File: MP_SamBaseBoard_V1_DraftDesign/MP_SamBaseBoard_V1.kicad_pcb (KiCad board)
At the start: 2 copper layers, 175 x 130.2 mm, 265 parts, among them J1 MOTOR-A_CONN, J10 P1_CONN, J11 I2C_CONN, J12 I2C_CONN, J13 SAM_SWD, J14 WS2812_EXT, J15 PWR_JACK, J16 USB_B_Micro, J17 BATT_CONN, J2 MOTOR-B_CONN, J3 Adafruit_Feather_CONN, J4 uSD_Card, J5 Conn_01x02, J6 Conn_01x02, J7 SERVO_CONN, J8 P3_CONN, J9 P2_CONN, Q1 DMP3098L, SW1 RESET, SW2 3v3_PWR_SW, SW3 SW1, SW4 SW2, U1 ESP32-WROOM-32, U10 MPU-6050, U11 IRFHM9331PbF, U12 BD5291FVE-GTR, U2 ATSAMD51J19A-A, U3 74LVC1G125, U4 TPS62135, U5 TPS62086, U6 MAX98357AETE, U7 DRV8833RTY, U8 HDC1080, U9 MCP73871-1CC, Y1 Crystal

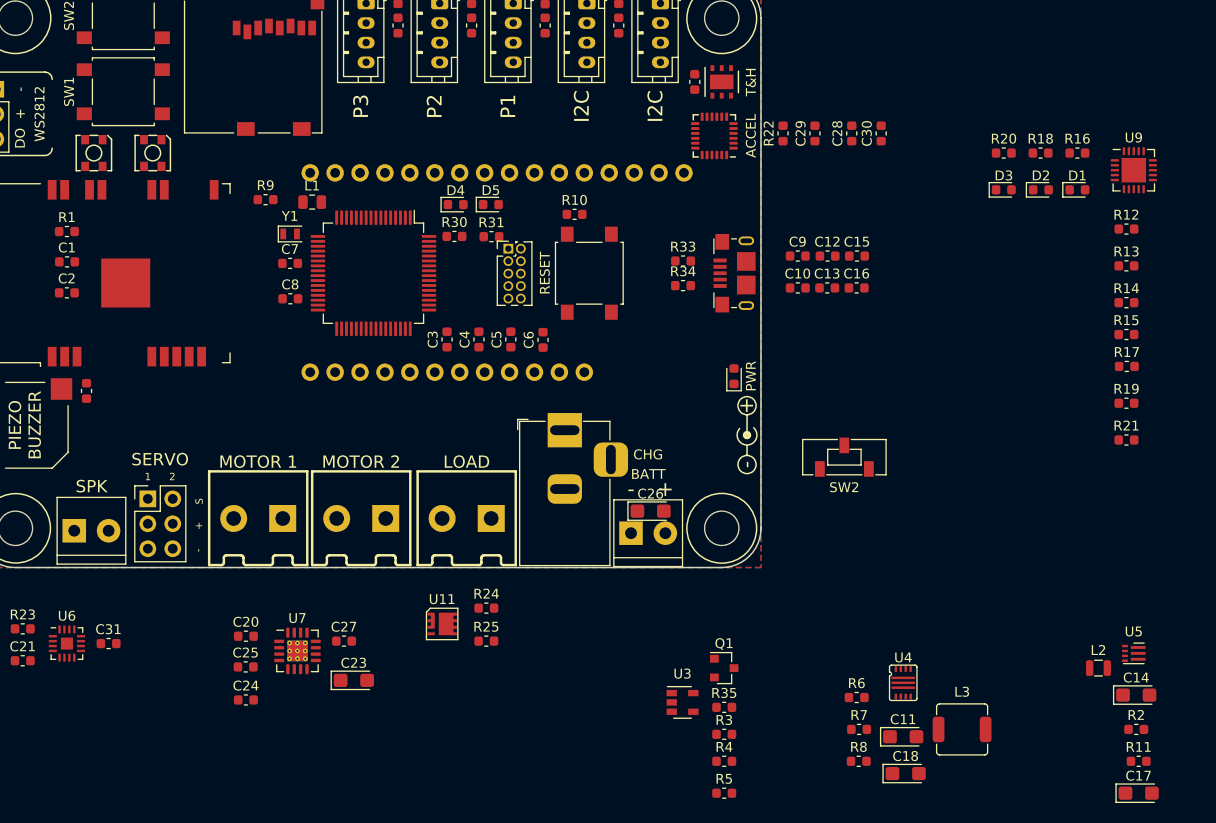
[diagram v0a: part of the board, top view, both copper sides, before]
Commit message: Progress in PCB, QSPI flash not complete in schematics
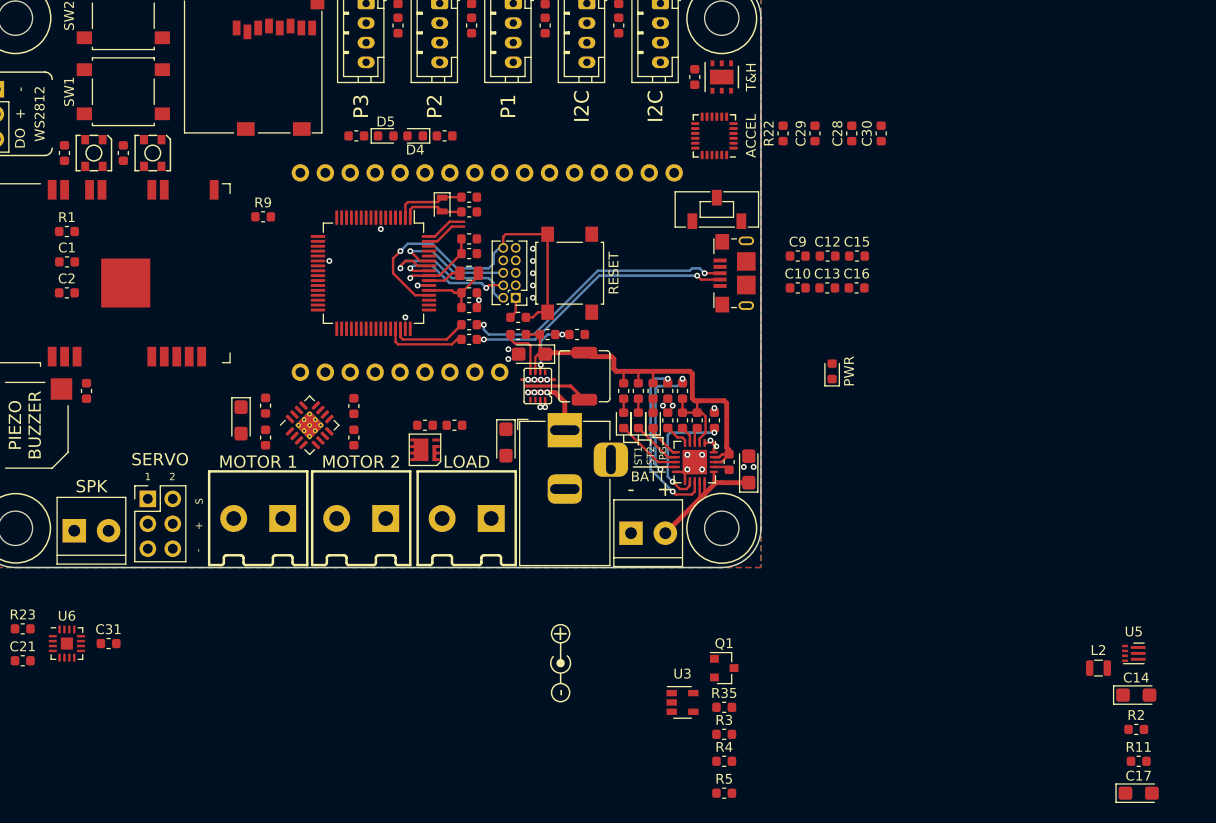
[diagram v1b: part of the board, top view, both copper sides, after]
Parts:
- added C42: 1uF, Capacitor_SMD:C_0603_1608Metric, F.Cu at (178.8, 180.5)
- added C43: 1uF, Capacitor_SMD:C_0603_1608Metric, F.Cu at (184.8, 180.5)
- J3: footprint GiraffeTech-Connector:Adafruit-Feather_WoMountPoint -> GiraffeTech-Connector:Adafruit-Feather_WoMountPoint_TypeA
- moved C18 57.3 mm to (226.4, 201.0), turned to 180 degrees
- moved R8 55.7 mm to (225.0, 199.0), turned to 180 degrees
- moved U9 53.7 mm to (243.0, 212.0), turned to 270 degrees
- moved L3 52.7 mm to (231.8, 203.2), turned to 90 degrees
- moved C11 50.4 mm to (223.8, 210.0), turned to 270 degrees
- moved R16 49.6 mm to (238.8, 204.8), turned to 270 degrees
- moved R7 49.5 mm to (231.0, 199.0)
- moved D1 49.2 mm to (238.8, 207.8), turned to 90 degrees
- moved R18 48.9 mm to (235.8, 204.8), turned to 270 degrees
- moved D2 48.6 mm to (235.8, 207.8), turned to 90 degrees
- moved R6 48.6 mm to (228.0, 199.0)
- moved U4 48.0 mm to (227.0, 204.2), turned to 180 degrees
- moved R13 47.0 mm to (241.8, 204.8), turned to 90 degrees
- moved R12 47.0 mm to (246.5, 212.0), turned to 270 degrees
- moved R14 46.8 mm to (241.8, 207.8), turned to 270 degrees
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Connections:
- J6 pad 1: Net-(J6-Pad1) -> GND
- J6 pad 2: GND -> Net-(J6-Pad2)
- U11 pad 1: Net-(J6-Pad1) -> Net-(J6-Pad2)
- U11 pad 2: Net-(J6-Pad1) -> Net-(J6-Pad2)
- U11 pad 3: Net-(J6-Pad1) -> Net-(J6-Pad2)
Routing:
- net +5V: track 0.00 -> 49.8 mm
- net ~RESET: track 0.00 -> 36.6 mm, vias 0 -> 1
- net Net-(J16-Pad3): track 0.00 -> 28.5 mm, vias 0 -> 2
- net Net-(J16-Pad2): track 0.00 -> 27.6 mm, vias 0 -> 2
- net PROG1: track 0.00 -> 18.1 mm, vias 0 -> 2
- net SWDIO: track 0.00 -> 16.7 mm, vias 0 -> 1
- net +BATT: track 0.00 -> 14.9 mm
- net ~TE: track 0.00 -> 13.9 mm, vias 0 -> 2
- net VIN: track 0.00 -> 13.5 mm, vias 0 -> 4
- net PROG3: track 0.00 -> 12.9 mm, vias 0 -> 2
- net SWO: track 0.00 -> 12.7 mm, vias 0 -> 1
- net SWCLK: track 0.00 -> 12.7 mm, vias 0 -> 2
- net GND: track 0.00 -> 11.3 mm, vias 0 -> 27
- net +3V3: track 0.00 -> 10.2 mm, vias 0 -> 1
- net USB_DM: track 0.00 -> 8.36 mm
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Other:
- board text added: "PG"
- board text added: "ST1"
- board text added: "ST2"

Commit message: update
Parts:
- added U13: SST25VF016B-50-4C-S2AF, Package_SO:SOIC-8_5.275x5.275mm_P1.27mm, F.Cu at (199.5, 192.8)
- J3: footprint GiraffeTech-Connector:Adafruit-Feather_WoMountPoint_TypeA -> GiraffeTech-Connector:Adafruit-Feather_WoMountPoint_TypeB
- moved C17 67.2 mm to (237.5, 201.7), turned to 180 degrees
- moved R11 56.9 mm to (248.0, 202.2)
- moved R2 55.7 mm to (248.0, 200.5)
- moved L2 52.9 mm to (241.5, 201.7), turned to 180 degrees
- moved U5 52.4 mm to (244.8, 201.5), turned to 180 degrees
- moved C14 51.5 mm to (247.2, 204.2)
- moved R4 48.8 mm to (235.8, 194.8)
- moved R5 48.2 mm to (236.5, 198.5), turned to 270 degrees
- moved R3 44.7 mm to (235.8, 196.2), turned to 180 degrees
- moved R35 40.0 mm to (235.0, 198.5), turned to 90 degrees
- moved U3 38.1 mm to (239.2, 198.5)
- moved Q1 34.6 mm to (243.0, 198.5)
- moved C10 31.1 mm to (222.6, 198.1), turned to 270 degrees
- moved C15 19.1 mm to (248.0, 206.2)
- moved C9 19.1 mm to (248.0, 209.2)
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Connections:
- U3 pad 5: VCC -> +3V3
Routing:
- net +3V3: track 10.2 -> 53.0 mm
- net USB_ID: track 0.00 -> 32.4 mm, vias 0 -> 2
- net AREF: track 0.00 -> 30.0 mm
- net CHG_OUT: track 2.27 -> 30.9 mm, vias 2 -> 6
- net Adf_A0_DAC0: track 0.00 -> 21.9 mm
- net VIN: track 13.5 -> 35.1 mm, vias 4 -> 5
- net 3v3_EN: track 0.00 -> 19.4 mm, vias 0 -> 2
- net Adf_D12: track 0.00 -> 18.9 mm
- net Adf_D11: track 0.00 -> 13.0 mm
- net Adf_D10: track 0.00 -> 11.0 mm
- net Net-(Q1-Pad1): track 0.00 -> 10.5 mm
- net Adf_D9: track 0.00 -> 7.12 mm, vias 0 -> 1
- net GND: track 11.3 -> 17.3 mm, vias 27 -> 68
- net +5V: track 49.8 -> 55.7 mm
- net VBUS: track 0.00 -> 5.85 mm
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- added copper zone on F.Cu, net CHG_OUT
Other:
- board text added: "ON"
- board text added: "RST"

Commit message: update
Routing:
- net +5V: track 55.7 -> 130.4 mm, vias 0 -> 3
- net VIN: track 35.1 -> 81.7 mm
- net PROG1: track 17.8 -> 20.1 mm
- net PROG3: track 13.7 -> 12.5 mm
- net ~TE: track 13.1 -> 13.6 mm
- net GND: vias 68 -> 85

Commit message: update
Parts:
- moved C27 5.30 mm to (194.0, 205.5)
- moved C20 2.68 mm to (210.5, 207.8), turned to 270 degrees
- moved C24 0.79 mm to (199.5, 210.2), turned to 180 degrees
- moved C25 0.79 mm to (208.0, 210.2), turned to 180 degrees
- moved C23 0.56 mm to (196.2, 208.0), turned to 180 degrees
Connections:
- J1 pad 1: Net-(C24-Pad2) -> Net-(C24-Pad1)
- J1 pad 2: Net-(C24-Pad1) -> Net-(C24-Pad2)
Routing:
- net Adf_D11: track 13.0 -> 36.2 mm, vias 0 -> 1
- net VIN: track 81.7 -> 98.0 mm, vias 5 -> 7
- net Net-(C24-Pad1): track 0.00 -> 12.9 mm
- net Net-(C25-Pad2): track 0.00 -> 12.9 mm
- net Net-(C25-Pad1): track 0.00 -> 12.6 mm
- net Net-(C24-Pad2): track 0.00 -> 12.6 mm
- net GND: track 17.3 -> 20.9 mm, vias 85 -> 89
- net +5V: track 130.4 -> 126.9 mm

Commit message: update & looking forward to be 4-layer
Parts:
- moved C2 24.1 mm to (199.0, 181.2), turned to 90 degrees
- moved C1 19.8 mm to (195.8, 181.2), turned to 90 degrees
- moved R1 15.5 mm to (192.8, 181.2), turned to 90 degrees
- moved C20 5.93 mm to (205.3, 204.9), turned to 180 degrees
- moved C27 4.37 mm to (198.0, 207.2), turned to 180 degrees
- moved C23 3.72 mm to (198.8, 205.2)
- moved R24 2.66 mm to (220.2, 208.5), turned to 90 degrees
- moved R25 1.82 mm to (221.8, 208.5), turned to 270 degrees
- moved R9 1.75 mm to (200.8, 187.0)
- moved U11 0.78 mm to (217.8, 208.7), turned to 90 degrees
- moved R33 0.25 mm to (220.0, 198.2)
- moved R34 0.25 mm to (220.0, 199.8)
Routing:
- net +3V3: track 53.0 -> 153.1 mm, vias 1 -> 5
- net Adf_D6: track 0.00 -> 29.1 mm
- net Adf_D9: track 7.12 -> 35.4 mm, vias 1 -> 2
- net SPI_MISO: track 0.00 -> 22.3 mm, vias 0 -> 1
- net Adf_D10: track 11.0 -> 31.5 mm, vias 0 -> 1
- net SPI_SCK: track 0.00 -> 18.9 mm, vias 0 -> 1
- net SPI_MOSI: track 0.00 -> 18.9 mm, vias 0 -> 1
- net Adf_D12: track 18.9 -> 36.9 mm, vias 0 -> 1
- net Adf_D5: track 0.00 -> 15.6 mm
- net GND: track 20.9 -> 31.5 mm, vias 89 -> 107
- net QSPI_IO3: track 0.00 -> 9.50 mm
- net Net-(J6-Pad2): track 0.00 -> 9.20 mm
- net QSPI_IO2: track 0.00 -> 7.76 mm
- net QSPI_IO1: track 0.00 -> 6.00 mm
- net VIN: track 98.0 -> 103.1 mm, vias 7 -> 8
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
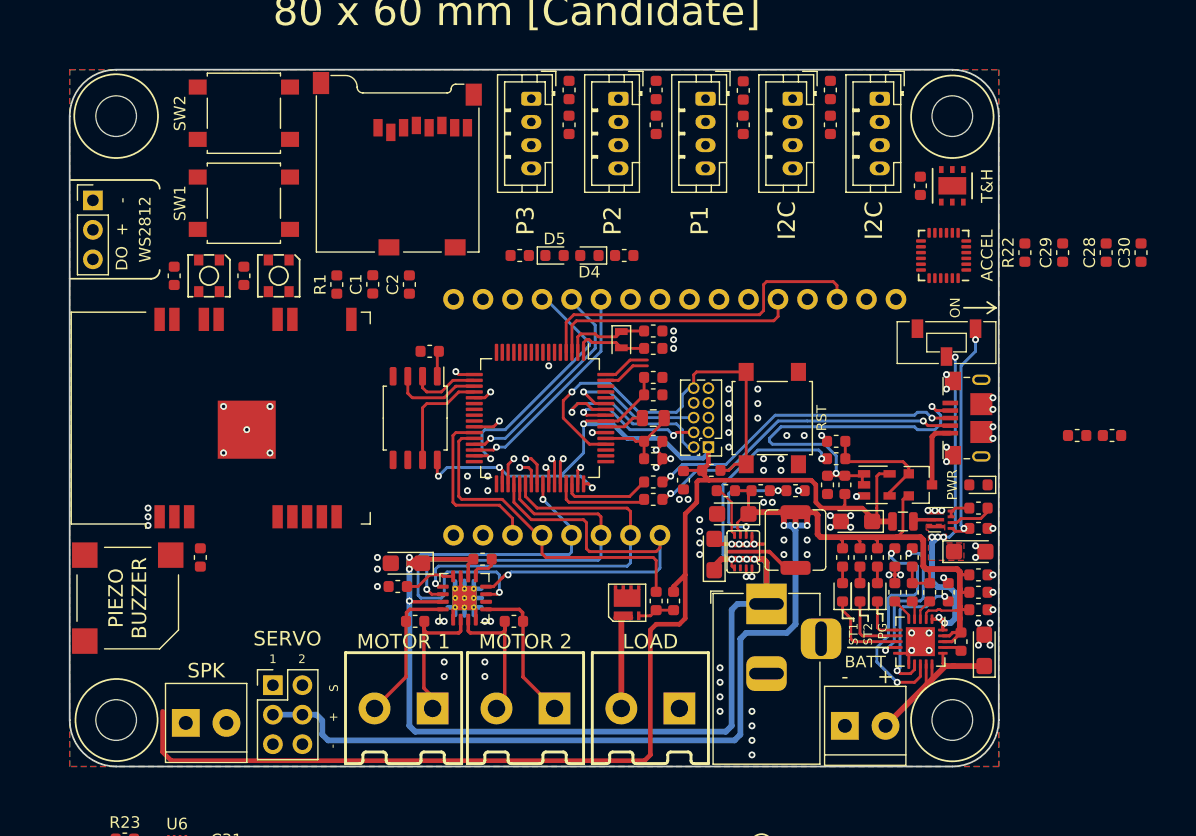
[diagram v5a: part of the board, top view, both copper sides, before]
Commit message: update to 4-layer
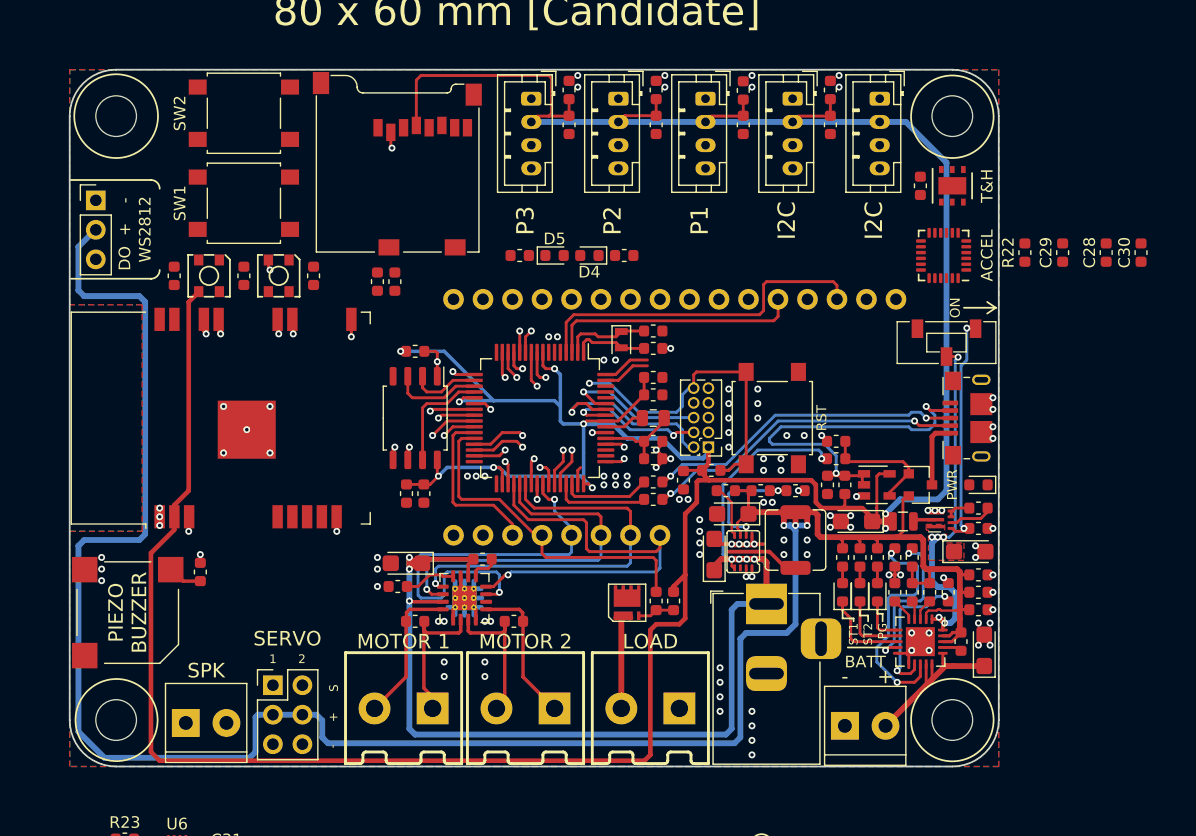
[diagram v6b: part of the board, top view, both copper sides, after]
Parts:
- moved C16 59.5 mm to (200.2, 199.2), turned to 270 degrees
- moved C13 58.0 mm to (198.8, 199.2), turned to 270 degrees
- moved D6 6.00 mm to (187.8, 180.5)
- moved D7 6.00 mm to (181.8, 180.5)
- moved R1 2.14 mm to (190.8, 180.5)
- moved C2 1.27 mm to (197.8, 181.0)
- moved BZ1 1.25 mm to (174.8, 209.5)
- moved R32 1.25 mm to (181.0, 206.0)
- moved R9 1.25 mm to (199.5, 187.0)
- moved C1 0.47 mm to (196.2, 181.0)
- moved J14 0.25 mm to (172.0, 174.0)
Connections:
- C34 pad 1: +5V -> +3V3
- C35 pad 1: +5V -> +3V3
- C36 pad 1: +5V -> +3V3
- C37 pad 1: +5V -> +3V3
- C38 pad 1: +5V -> +3V3
- C39 pad 1: +5V -> +3V3
- C40 pad 1: +5V -> +3V3
- C41 pad 1: +5V -> +3V3
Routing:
- net +3V3: track 153.1 -> 335.9 mm, vias 5 -> 9
- net +5V: track 126.9 -> 202.6 mm
- net WS2812_INT: track 0.00 -> 56.7 mm, vias 0 -> 2
- net D0_RxD0: track 2.27 -> 50.1 mm, vias 1 -> 2
- net Adf_D4: track 2.37 -> 47.4 mm
- net D1_TxD0: track 2.27 -> 47.3 mm, vias 1 -> 2
- net SPI_SCK: track 18.9 -> 59.7 mm, vias 1 -> 2
- net Adf_D8: track 1.52 -> 40.9 mm, vias 1 -> 2
- net Adf_D5: track 15.6 -> 50.7 mm, vias 0 -> 1
- net Adf_D13: track 2.37 -> 35.8 mm, vias 1 -> 2
- net Adf_D3: track 2.27 -> 35.5 mm, vias 1 -> 2
- net Adf_D2: track 2.87 -> 34.8 mm, vias 1 -> 2
- net Adf_D7: track 0.00 -> 30.7 mm, vias 0 -> 1
- net SPI_MOSI: track 18.9 -> 48.5 mm, vias 1 -> 2
- net Adf_A3: track 0.00 -> 20.9 mm, vias 0 -> 1
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- added copper zone on In1.Cu, net GND
- added copper zone on In2.Cu, net GND
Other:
- copper layers 2 -> 4

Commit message: update
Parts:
- moved D5 31.5 mm to (239.2, 193.8), turned to 90 degrees
- moved D4 30.7 mm to (241.2, 193.8), turned to 90 degrees
- moved R31 29.2 mm to (235.8, 189.2)
- moved R30 21.8 mm to (235.8, 190.8), turned to 180 degrees
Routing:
- net I2C_SDA: track 4.11 -> 58.9 mm, vias 0 -> 1
- net I2C_SCL: track 4.69 -> 57.6 mm, vias 0 -> 1
- net SAM_TxLED: track 0.00 -> 36.2 mm, vias 0 -> 2
- net USB_PWR_SEL: track 3.12 -> 34.8 mm, vias 1 -> 2
- net ~RESET: track 37.1 -> 67.0 mm, vias 2 -> 1
- net SAM_RxLED: track 2.77 -> 29.3 mm, vias 1 -> 2
- net Adf_A2: track 2.27 -> 27.8 mm
- net Adf_A1_DAC1: track 2.47 -> 26.8 mm
- net +3V3: track 335.9 -> 356.8 mm
- net Net-(D4-Pad1): track 0.00 -> 9.99 mm
- net USB_ID: track 32.4 -> 22.8 mm
- net Net-(D5-Pad1): track 0.00 -> 7.69 mm
- net VIN: track 103.6 -> 106.8 mm
- net SWO: track 12.7 -> 14.5 mm
- net WS2812_INT: track 56.7 -> 57.6 mm
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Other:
- board text added: "PWR SW"
- board text added: "Rx"
- board text added: "Tx"

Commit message: update
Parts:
- moved C19 110.4 mm to (253.8, 166.0)
- moved C32 110.4 mm to (253.8, 169.5)
- moved C33 110.4 mm to (262.0, 171.0)
- moved MK1 110.4 mm to (253.8, 160.8)
- moved R26 110.4 mm to (257.5, 162.2)
- moved R27 110.4 mm to (257.5, 165.5)
- moved R28 110.4 mm to (261.0, 162.2)
- moved R29 110.4 mm to (258.2, 169.2)
- moved U12 110.4 mm to (262.0, 166.8)
- moved C1 39.8 mm to (235.8, 186.2), turned to 0 degrees
- moved C2 38.6 mm to (235.8, 187.8), turned to 0 degrees
- moved R23 24.3 mm to (182.2, 206.0), turned to 90 degrees
- moved U6 23.8 mm to (185.2, 207.5), turned to 270 degrees
- moved C21 22.8 mm to (181.5, 210.5), turned to 180 degrees
- moved C31 21.6 mm to (181.5, 209.0), turned to 180 degrees
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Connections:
- U6 pad 16: GND -> D1_TxD0
- U6 pad 17: (no net) -> GND
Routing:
- net Adf_A3: track 20.6 -> 87.8 mm
- net Adf_A1_DAC1: track 26.8 -> 92.8 mm
- net SPI_MISO: track 22.6 -> 81.6 mm, vias 1 -> 3
- net D1_TxD0: track 47.1 -> 90.0 mm, vias 2 -> 3
- net +3V3: track 356.8 -> 383.1 mm
- net Adf_A4: track 15.2 -> 41.4 mm
- net SPI_SCK: track 59.7 -> 85.6 mm, vias 2 -> 3
- net SPI_MOSI: track 48.5 -> 72.8 mm, vias 2 -> 3
- net VIN: track 106.8 -> 85.1 mm
- net Adf_A2: track 27.8 -> 48.1 mm
- net Adf_A0_DAC0: track 21.9 -> 40.9 mm
- net Adf_D11: track 34.3 -> 51.5 mm, vias 1 -> 2
- net Adf_D10: track 31.6 -> 45.7 mm, vias 1 -> 2
- net Net-(J5-Pad2): track 0.00 -> 12.0 mm
- net Net-(J5-Pad1): track 0.00 -> 12.0 mm
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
